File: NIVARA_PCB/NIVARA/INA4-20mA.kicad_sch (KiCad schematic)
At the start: 0 parts

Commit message: avance
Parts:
- added C8: 100nF, PCM_Capacitor_SMD_AKL:C_0603_1608Metric, symbol PCM_Capacitor_AKL:C_0603
- added R7: 150R, symbol Device:R
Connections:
- net IN_1: now also C8.2, R7.1
- new net GND: C8.1, R7.2

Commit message: ACTUALIZACION
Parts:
- C8: PART NUMBERT (none) -> CC0603KRX7R9BB104
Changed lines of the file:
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@@
 			)
 		)
-		(property "PART NUMBERT" ""
+		(property "PART NUMBERT" "CC0603KRX7R9BB104"
 			(at 49.53 41.91 0)
 			(effects

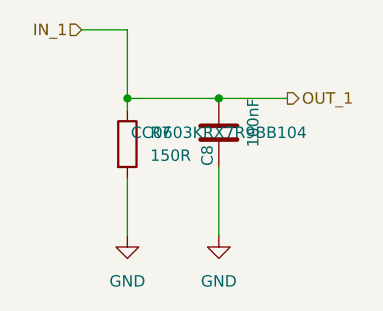
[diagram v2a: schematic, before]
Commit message: Se organizaron componentes en el area de PCB
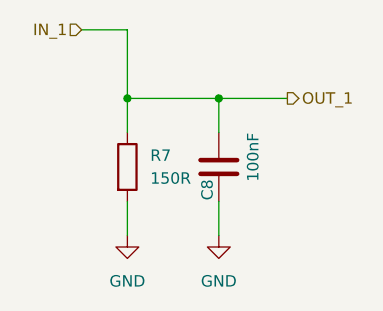
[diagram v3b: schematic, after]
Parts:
- R7: footprint (none) -> PCM_Resistor_SMD_AKL:R_0603_1608Metric; PART NUMBERT (none) -> RC0603FR-07150RL
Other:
- moved on the sheet: C8, R7
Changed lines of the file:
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@@
 	(wire
 		(pts
-			(xy 39.37 39.37) (xy 39.37 38.1)
+			(xy 39.37 41.91) (xy 39.37 38.1)
 		)
 		(stroke
@@
 	(wire
 		(pts
-			(xy 49.53 53.34) (xy 49.53 45.72)
-		)
-		(stroke
-			(width 0)
-			(type default)
-		)
-	)
-	(wire
-		(pts
-			(xy 39.37 53.34) (xy 39.37 46.99)
+			(xy 49.53 53.34) (xy 49.53 49.53)
+		)
+		(stroke
+			(width 0)
+			(type default)
+		)
+	)
+	(wire
+		(pts
+			(xy 39.37 53.34) (xy 39.37 49.53)
 		)
 		(stroke
@@
 		(pts
 			(xy 49.53 38.1) (xy 57.15 38.1)
+		)
+		(stroke
+			(width 0)
+			(type default)
+		)
+	)
+	(wire
+		(pts
+			(xy 49.53 41.91) (xy 49.53 38.1)
 		)
 		(stroke
@@
 	(symbol
 		(lib_id "PCM_Capacitor_AKL:C_0603")
-		(at 49.53 41.91 180)
+		(at 49.53 45.72 180)
 		(unit 1)
 		(exclude_from_sim no)
@@
 		(dnp no)
 		(property "Reference" "C8"
-			(at 48.26 44.45 90)
+			(at 48.26 48.26 90)
 			(effects
 				(font
@@
 		)
 		(property "Value" "100nF"
-			(at 53.34 38.1 90)
+			(at 53.34 41.91 90)
 			(effects
 				(font
@@
 		)
 		(property "Footprint" "PCM_Capacitor_SMD_AKL:C_0603_1608Metric"
-			(at 48.5648 38.1 0)
+			(at 48.5648 41.91 0)
 			(effects
 				(font
@@
 		)
 		(property "Datasheet" "~"
-			(at 49.53 41.91 0)
+			(at 49.53 45.72 0)
 			(effects
 				(font
@@
 		)
 		(property "Description" "SMD 0603 MLCC capacitor, Alternate KiCad Library"
-			(at 49.53 41.91 0)
+			(at 49.53 45.72 0)
 			(effects
 				(font
@@
 		)
 		(property "PART NUMBERT" "CC0603KRX7R9BB104"
-			(at 49.53 41.91 0)
-			(effects
-				(font
-					(size 1.27 1.27)
-				)
+			(at 49.53 45.72 0)
+			(effects
+				(font
+					(size 1.27 1.27)
+				)
+				(hide yes)
 			)
 		)
@@
 	(symbol
 		(lib_id "Device:R")
-		(at 39.37 43.18 0)
+		(at 39.37 45.72 0)
 		(unit 1)
 		(exclude_from_sim no)
@@
 		(fields_autoplaced yes)
 		(property "Reference" "R7"
-			(at 41.91 41.9099 0)
+			(at 41.91 44.4499 0)
 			(effects
 				(font
@@
 		)
 		(property "Value" "150R"
-			(at 41.91 44.4499 0)
+			(at 41.91 46.9899 0)
 			(effects
 				(font
@@
 			)
 		)
-		(property "Footprint" ""
-			(at 37.592 43.18 90)
+		(property "Footprint" "PCM_Resistor_SMD_AKL:R_0603_1608Metric"
+			(at 37.592 45.72 90)
 			(effects
 				(font
@@
 		)
 		(property "Datasheet" "~"
-			(at 39.37 43.18 0)
+			(at 39.37 45.72 0)
 			(effects
 				(font
@@
 		)
 		(property "Description" "Resistor"
-			(at 39.37 43.18 0)
-			(effects
-				(font
+			(at 39.37 45.72 0)
+			(effects
+				(font
+					(size 1.27 1.27)
+				)
+				(hide yes)
+			)
+		)
+		(property "PART NUMBERT" "RC0603FR-07150RL"
+			(at 39.37 45.72 0)
+			(effects
+				(font
